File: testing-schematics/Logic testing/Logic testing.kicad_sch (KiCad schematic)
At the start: 42 parts, among them J1 External Box, J2 Aux Wire, J4 Lame Tab, J5 Test Output, K1 G6K-2, K2 G6K-2, K3 G6K-2, K4 G6K-2, K5 G6K-2, P1 USB_C_Plug_USB2.0, Q1 BC547, Q2 BC547, Q3 BC547, Q4 BC547, SW1 SW_SPDT, SW2 SW_DP3T, SW3 SW_Push, U1 ESP32-C6-MINI-1, U2 TPS62840DLCR

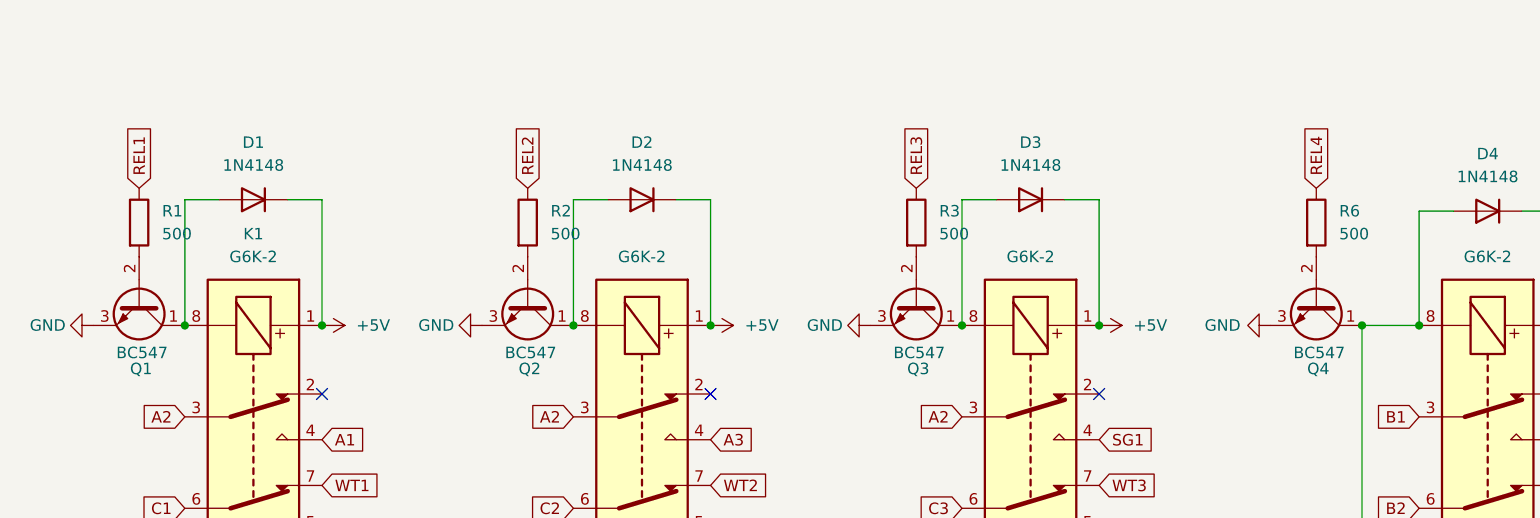
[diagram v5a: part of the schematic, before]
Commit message: Work on footprints, suppliers, BOM
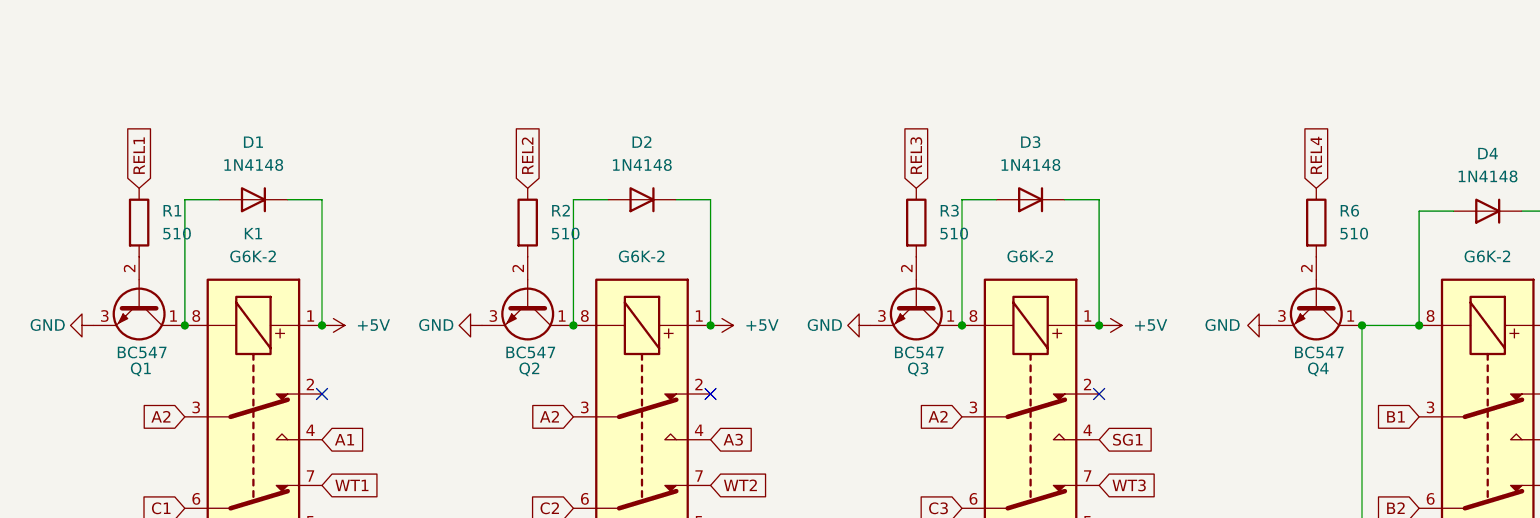
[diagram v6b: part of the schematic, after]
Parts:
- C1, C2: footprint (none) -> Capacitor_SMD:C_0805_2012Metric_Pad1.18x1.45mm_HandSolder
- C3: footprint (none) -> Capacitor_SMD:C_0603_1608Metric_Pad1.08x0.95mm_HandSolder
- K1, K2, K3, K4, K5: footprint (none) -> Relay_SMD:Relay_DPDT_Omron_G6K-2F
- L1: footprint (none) -> Inductor_SMD:L_1008_2520Metric_Pad1.43x2.20mm_HandSolder
- P1: footprint (none) -> Connector_USB:USB_C_Receptacle_GCT_USB4105-xx-A_16P_TopMnt_Horizontal
- R1, R2, R3, R6: value 500 -> 510; footprint Resistor_THT:R_Axial_DIN0204_L3.6mm_D1.6mm_P7.62mm_Horizontal -> Resistor_SMD:R_1206_3216Metric_Pad1.30x1.75mm_HandSolder
- R10: footprint (none) -> Resistor_THT:R_Axial_DIN0204_L3.6mm_D1.6mm_P7.62mm_Horizontal
- R11, R12, R13, R14, R15, R8, R9: footprint (none) -> Resistor_SMD:R_1206_3216Metric_Pad1.30x1.75mm_HandSolder
- R4, R5, R7: footprint Resistor_THT:R_Axial_DIN0204_L3.6mm_D1.6mm_P7.62mm_Horizontal -> Resistor_SMD:R_1206_3216Metric_Pad1.30x1.75mm_HandSolder
- SW1: footprint (none) -> Button_Switch_SMD:SW_SPDT_CK_JS102011SAQN
- SW2: footprint (none) -> Button_Switch_SMD:SW_SP3T_PCM13
- SW3: footprint (none) -> Button_Switch_THT:SW_PUSH-12mm
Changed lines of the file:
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@@
 			)
 		)
-		(property "Footprint" "Resistor_THT:R_Axial_DIN0204_L3.6mm_D1.6mm_P7.62mm_Horizontal"
+		(property "Footprint" "Resistor_SMD:R_1206_3216Metric_Pad1.30x1.75mm_HandSolder"
 			(at 168.402 80.01 90)
 			(effects
@@
 			)
 		)
-		(property "Footprint" "Resistor_THT:R_Axial_DIN0204_L3.6mm_D1.6mm_P7.62mm_Horizontal"
+		(property "Footprint" "Resistor_SMD:R_1206_3216Metric_Pad1.30x1.75mm_HandSolder"
 			(at 191.262 85.09 90)
 			(effects
@@
 			)
 		)
-		(property "Footprint" ""
+		(property "Footprint" "Resistor_SMD:R_1206_3216Metric_Pad1.30x1.75mm_HandSolder"
 			(at 95.758 142.24 90)
 			(effects
@@
 			)
 		)
-		(property "Footprint" ""
+		(property "Footprint" "Capacitor_SMD:C_0805_2012Metric_Pad1.18x1.45mm_HandSolder"
 			(at 74.6252 118.11 0)
 			(effects
@@
 			)
 		)
-		(property "Footprint" ""
+		(property "Footprint" "Resistor_SMD:R_1206_3216Metric_Pad1.30x1.75mm_HandSolder"
 			(at 69.85 23.368 90)
 			(effects
@@
 			)
 		)
-		(property "Footprint" ""
+		(property "Footprint" "Relay_SMD:Relay_DPDT_Omron_G6K-2F"
 			(at 157.48 55.88 0)
 			(effects
@@
 			)
 		)
-		(property "Footprint" ""
+		(property "Footprint" "Button_Switch_SMD:SW_SP3T_PCM13"
 			(at 42.545 19.685 0)
 			(effects
@@
 			)
 		)
-		(property "Footprint" ""
+		(property "Footprint" "Resistor_THT:R_Axial_DIN0204_L3.6mm_D1.6mm_P7.62mm_Horizontal"
 			(at 28.702 134.62 90)
 			(effects
@@
 			)
 		)
-		(property "Footprint" ""
+		(property "Footprint" "Capacitor_SMD:C_0603_1608Metric_Pad1.08x0.95mm_HandSolder"
 			(at 87.9348 146.05 0)
 			(effects
@@
 			)
 		)
-		(property "Footprint" ""
+		(property "Footprint" "Inductor_SMD:L_1008_2520Metric_Pad1.43x2.20mm_HandSolder"
 			(at 69.85 110.49 0)
 			(effects
@@
 			)
 		)
-		(property "Footprint" ""
+		(property "Footprint" "Resistor_SMD:R_1206_3216Metric_Pad1.30x1.75mm_HandSolder"
 			(at 79.248 93.98 90)
 			(effects
@@
 			)
 		)
-		(property "Footprint" "Resistor_THT:R_Axial_DIN0204_L3.6mm_D1.6mm_P7.62mm_Horizontal"
+		(property "Footprint" "Resistor_SMD:R_1206_3216Metric_Pad1.30x1.75mm_HandSolder"
 			(at 179.832 82.55 90)
 			(effects
@@
 			)
 		)
-		(property "Value" "500"
+		(property "Value" "510"
 			(at 147.32 35.5599 0)
 			(effects
@@
 			)
 		)
-		(property "Footprint" "Resistor_THT:R_Axial_DIN0204_L3.6mm_D1.6mm_P7.62mm_Horizontal"
+		(property "Footprint" "Resistor_SMD:R_1206_3216Metric_Pad1.30x1.75mm_HandSolder"
 			(at 143.002 34.29 90)
 			(effects
@@
 			)
 		)
-		(property "Footprint" ""
+		(property "Footprint" "Capacitor_SMD:C_0805_2012Metric_Pad1.18x1.45mm_HandSolder"
 			(at 28.9052 110.49 0)
 			(effects
@@
 			)
 		)
-		(property "Footprint" ""
+		(property "Footprint" "Button_Switch_THT:SW_PUSH-12mm"
 			(at 72.39 85.09 0)
 			(effects
@@
 			)
 		)
-		(property "Footprint" ""
+		(property "Footprint" "Relay_SMD:Relay_DPDT_Omron_G6K-2F"
 			(at 251.46 55.88 0)
 			(effects
@@
 			)
 		)
-		(property "Footprint" ""
+		(property "Footprint" "Connector_USB:USB_C_Receptacle_GCT_USB4105-xx-A_16P_TopMnt_Horizontal"
 			(at 105.41 115.57 0)
 			(effects
@@
 			)
 		)
-		(property "Footprint" ""
+		(property "Footprint" "Button_Switch_SMD:SW_SPDT_CK_JS102011SAQN"
 			(at 19.05 36.83 0)
 			(effects
@@
 			)
 		)
-		(property "Footprint" ""
+		(property "Footprint" "Relay_SMD:Relay_DPDT_Omron_G6K-2F"
 			(at 251.46 91.44 0)
 			(effects
@@
 			)
 		)
-		(property "Footprint" ""
+		(property "Footprint" "Resistor_SMD:R_1206_3216Metric_Pad1.30x1.75mm_HandSolder"
 			(at 26.67 32.258 90)
 			(effects
@@
 			)
 		)
-		(property "Footprint" ""
+		(property "Footprint" "Resistor_SMD:R_1206_3216Metric_Pad1.30x1.75mm_HandSolder"
 			(at 69.85 24.892 90)
 			(effects
@@
 			)
 		)
-		(property "Footprint" ""
+		(property "Footprint" "Resistor_SMD:R_1206_3216Metric_Pad1.30x1.75mm_HandSolder"
 			(at 120.65 107.188 90)
 			(effects
@@
 			)
 		)
-		(property "Footprint" ""
+		(property "Footprint" "Relay_SMD:Relay_DPDT_Omron_G6K-2F"
 			(at 114.3 55.88 0)
 			(effects
@@
 			)
 		)
-		(property "Footprint" ""
+		(property "Footprint" "Resistor_SMD:R_1206_3216Metric_Pad1.30x1.75mm_HandSolder"
 			(at 97.79 150.368 90)
 			(effects
@@
 			)
 		)
-		(property "Value" "500"
+		(property "Value" "510"
 			(at 190.5 35.5599 0)
 			(effects
@@
 			)
 		)
-		(property "Footprint" "Resistor_THT:R_Axial_DIN0204_L3.6mm_D1.6mm_P7.62mm_Horizontal"
+		(property "Footprint" "Resistor_SMD:R_1206_3216Metric_Pad1.30x1.75mm_HandSolder"
 			(at 186.182 34.29 90)
 			(effects
@@
 			)
 		)
-		(property "Footprint" ""
+		(property "Footprint" "Relay_SMD:Relay_DPDT_Omron_G6K-2F"
 			(at 200.66 55.88 0)
 			(effects
@@
 			)
 		)
-		(property "Value" "500"
+		(property "Value" "510"
 			(at 234.95 35.5599 0)
 			(effects
@@
 			)
 		)
-		(property "Footprint" "Resistor_THT:R_Axial_DIN0204_L3.6mm_D1.6mm_P7.62mm_Horizontal"
+		(property "Footprint" "Resistor_SMD:R_1206_3216Metric_Pad1.30x1.75mm_HandSolder"
 			(at 230.632 34.29 90)
 			(effects
@@
 			)
 		)
-		(property "Value" "500"
+		(property "Value" "510"
 			(at 104.14 35.5599 0)
 			(effects
@@
 			)
 		)
-		(property "Footprint" "Resistor_THT:R_Axial_DIN0204_L3.6mm_D1.6mm_P7.62mm_Horizontal"
+		(property "Footprint" "Resistor_SMD:R_1206_3216Metric_Pad1.30x1.75mm_HandSolder"
 			(at 99.822 34.29 90)
 			(effects

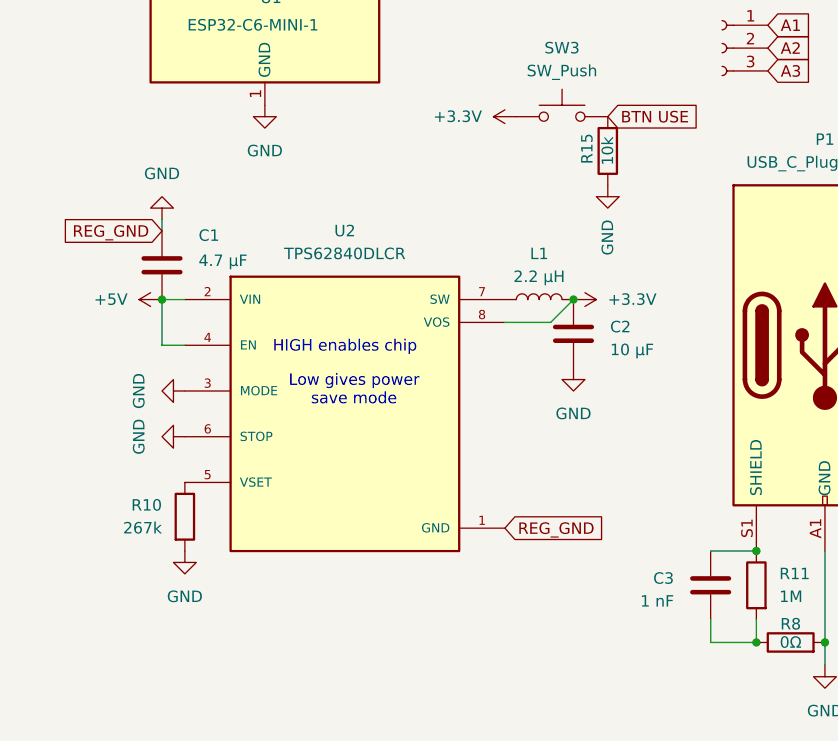
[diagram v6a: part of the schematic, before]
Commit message: Journal; BOM changes; PCB changes
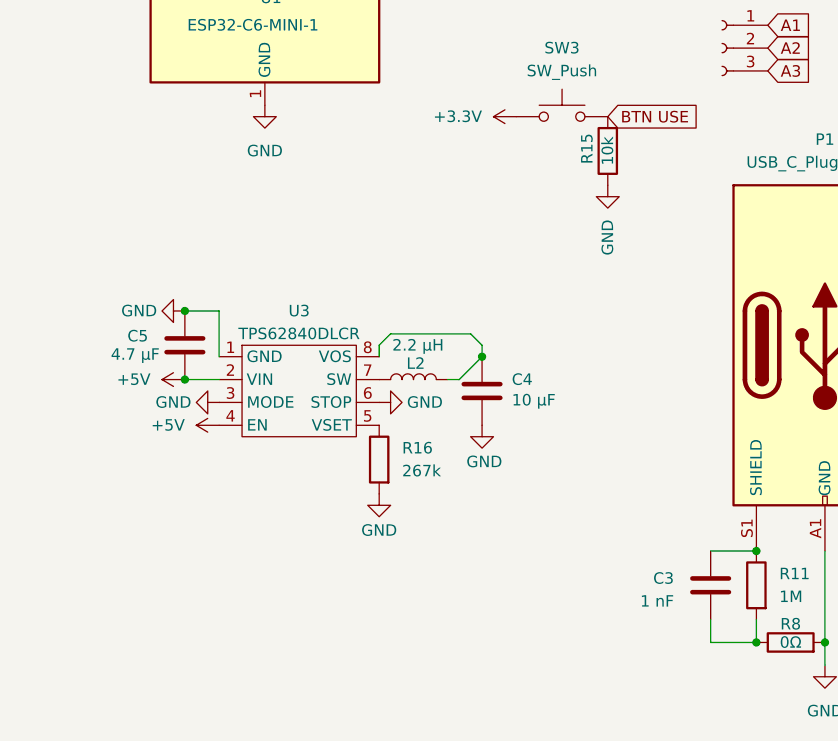
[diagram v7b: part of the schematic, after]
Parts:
- removed C1: 4.7 µF, Capacitor_SMD:C_0805_2012Metric_Pad1.18x1.45mm_HandSolder, symbol Device:C
- removed C2: 10 µF, Capacitor_SMD:C_0805_2012Metric_Pad1.18x1.45mm_HandSolder, symbol Device:C
- removed L1: 2.2 µH, Inductor_SMD:L_1008_2520Metric_Pad1.43x2.20mm_HandSolder, symbol Device:L
- removed R10: 267k, Resistor_THT:R_Axial_DIN0204_L3.6mm_D1.6mm_P7.62mm_Horizontal, symbol Device:R
- removed U2: TPS62840DLCR, TPS62840DLCR:SON50P200X150X100-8N, symbol Imports:TPS62840DLCR
- added C4: 10 µF, Capacitor_SMD:C_0805_2012Metric_Pad1.18x1.45mm_HandSolder, symbol Device:C
- added C5: 4.7 µF, Capacitor_SMD:C_0805_2012Metric_Pad1.18x1.45mm_HandSolder, symbol Device:C
- added L2: 2.2 µH, Inductor_SMD:L_1008_2520Metric_Pad1.43x2.20mm_HandSolder, symbol Device:L
- added R16: 267k, Resistor_THT:R_Axial_DIN0204_L3.6mm_D1.6mm_P7.62mm_Horizontal, symbol Device:R
- added U3: TPS62840DLCR, Package_SON:VSON-8_1.5x2mm_P0.5mm, symbol Custom:TPS62840DLC
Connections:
- net +5V: now also C5.2, U3.2 (VIN), U3.4 (EN)
- net GND: now also C4.2, C5.1, R16.2, U3.1 (GND), U3.3 (MODE), U3.6 (STOP)
- new net: C4.1, L2.2, U3.8 (VOS)
- new net: L2.1, U3.7 (SW)
- new net: R16.1, U3.5 (VSET)
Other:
- note removed: "HIGH enables chip"
- note removed: "Low gives power save mode"

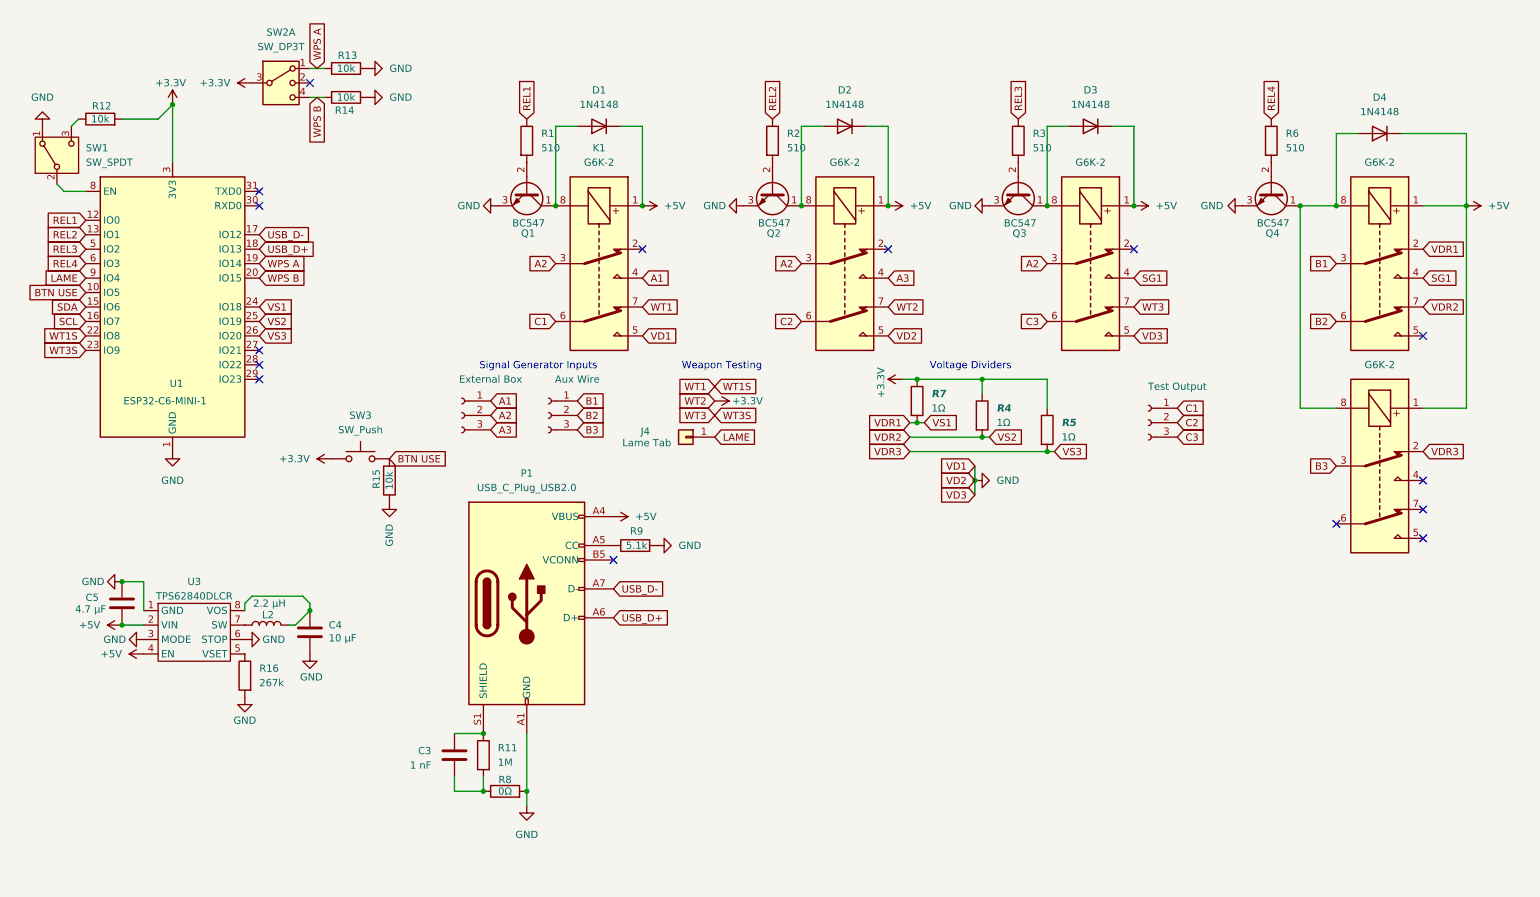
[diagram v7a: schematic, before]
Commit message: Worked on new power; Worked on display; Replaces ESP controller; Restructured schematic; Worked on PCB layout; Did journal
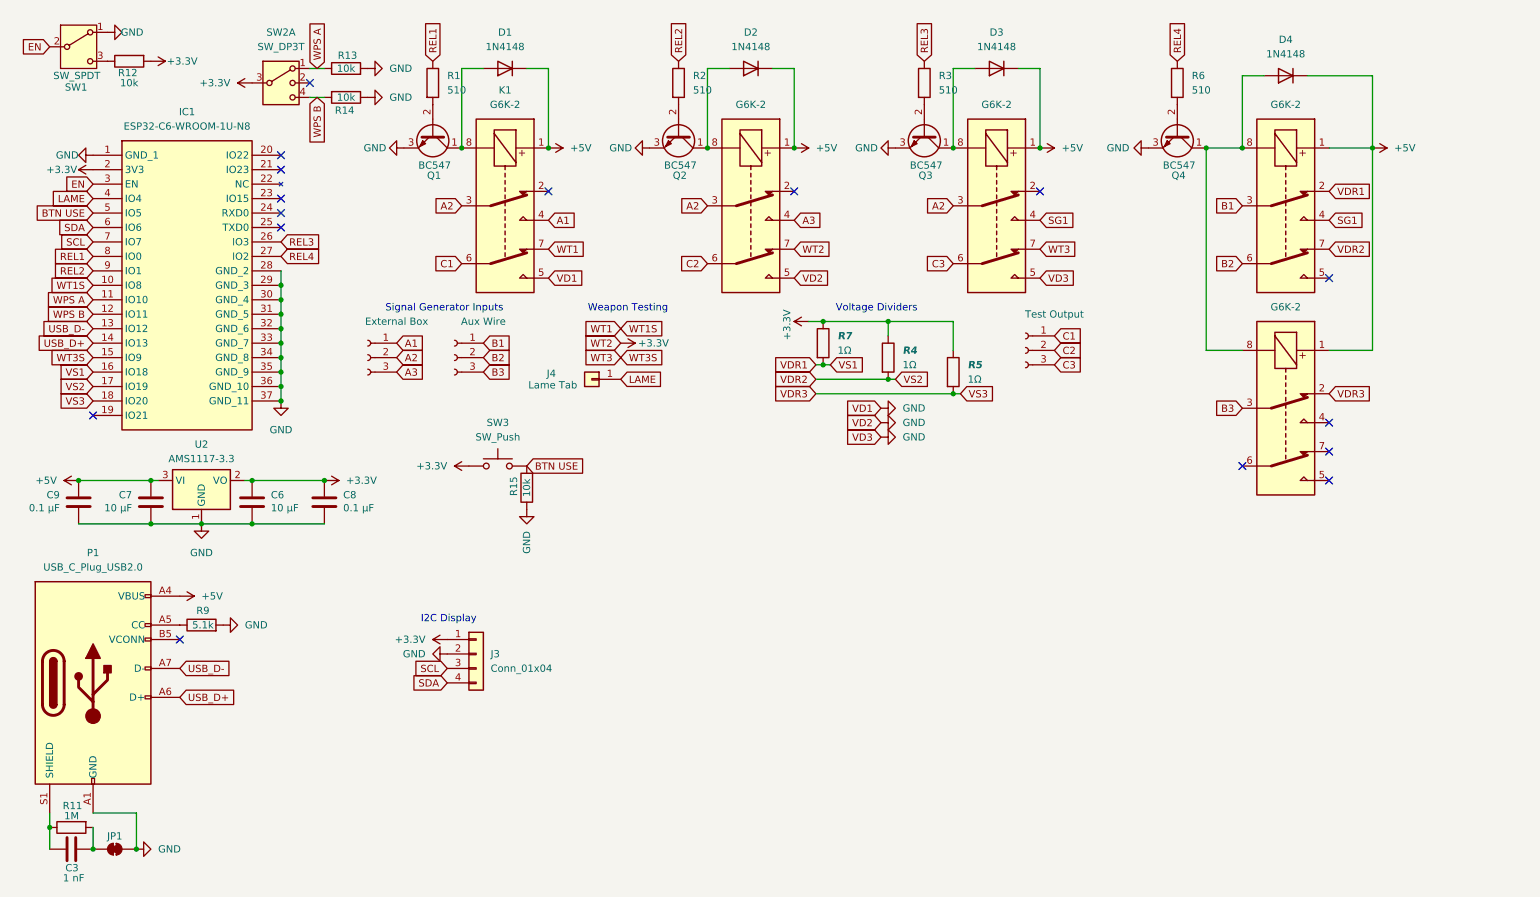
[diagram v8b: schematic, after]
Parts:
- removed C4: 10 µF, Capacitor_SMD:C_0805_2012Metric_Pad1.18x1.45mm_HandSolder, symbol Device:C
- removed C5: 4.7 µF, Capacitor_SMD:C_0805_2012Metric_Pad1.18x1.45mm_HandSolder, symbol Device:C
- removed L2: 2.2 µH, Inductor_SMD:L_1008_2520Metric_Pad1.43x2.20mm_HandSolder, symbol Device:L
- removed R16: 267k, Resistor_THT:R_Axial_DIN0204_L3.6mm_D1.6mm_P7.62mm_Horizontal, symbol Device:R
- removed R8: 0Ω, Resistor_SMD:R_1206_3216Metric_Pad1.30x1.75mm_HandSolder, symbol Device:R
- removed U1: ESP32-C6-MINI-1, RF_Module:ESP32-C6-MINI-1, symbol RF_Module:ESP32-C6-MINI-1
- removed U3: TPS62840DLCR, Package_SON:VSON-8_1.5x2mm_P0.5mm, symbol Custom:TPS62840DLC
- added C6, C7: 10 µF, Capacitor_SMD:C_0805_2012Metric_Pad1.18x1.45mm_HandSolder, symbol Device:C
- added C8, C9: 0.1 µF, Capacitor_SMD:C_0805_2012Metric_Pad1.18x1.45mm_HandSolder, symbol Device:C
- added IC1: ESP32-C6-WROOM-1U-N8, Importer:ESP32C6WROOM1UN8, symbol Importer:ESP32-C6-WROOM-1U-N8
- added J3: Conn_01x04, Connector_PinSocket_2.54mm:PinSocket_1x04_P2.54mm_Vertical, symbol Connector_Generic:Conn_01x04
- added JP1: SolderJumper_2_Closed, Jumper:SolderJumper-2_P1.3mm_Bridged_RoundedPad1.0x1.5mm, symbol Jumper:SolderJumper_2_Bridged
- added U2: AMS1117-3.3, Package_TO_SOT_SMD:SOT-223, symbol Regulator_Linear:AMS1117-3.3
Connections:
- net +3.3V: now also C6.1, C8.1, IC1.2 (3V3), J3.1 (Pin_1), U2.2 (VO)
- net +5V: now also C7.1, C9.1, U2.3 (VI)
- net BTN USE: now also IC1.5 (IO5)
- net GND: now also C6.2, C7.2, C8.2, C9.2, IC1.1 (GND_1), IC1.28 (GND_2), IC1.29 (GND_3), IC1.30 (GND_4), IC1.31 (GND_5), IC1.32 (GND_6), IC1.33 (GND_7), IC1.34 (GND_8), IC1.35 (GND_9), IC1.36 (GND_10), IC1.37 (GND_11), J3.2 (Pin_2), JP1.2 (B), U2.1 (GND)
- net LAME: now also IC1.4 (IO4)
- net REL1: now also IC1.8 (IO0)
- net REL2: now also IC1.9 (IO1)
- net REL3: now also IC1.26 (IO3)
- net REL4: now also IC1.27 (IO2)
- net SCL: now also IC1.7 (IO7), J3.3 (Pin_3)
- net SDA: now also IC1.6 (IO6), J3.4 (Pin_4)
- net USB_D+: now also IC1.14 (IO13)
- net USB_D-: now also IC1.13 (IO12)
- net VDR1: now also IC1.16 (IO18)
- net VDR2: now also IC1.17 (IO19)
- net VDR3: now also IC1.18 (IO20)
- net WPS A: now also IC1.11 (IO10)
- net WPS B: now also IC1.12 (IO11)
- net WT1: now also IC1.10 (IO8)
- net WT3: now also IC1.15 (IO9)
- net at C3.2, R11.2: now also JP1.1 (A)
- net EN: now reaches SW1.2 (B)
- net EN: now also IC1.3 (EN)
- no-connect marks 15 -> 16
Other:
- note added: "I2C Display"
- moved on the sheet: C3, D1, D2, D3, D4, J4, K1, P1, Q1, Q2, Q3, Q4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
